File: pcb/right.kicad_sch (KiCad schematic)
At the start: 119 parts, among them J201 OLED 0.96in I2C, Q201 AO3401A, Q202 AO3401A, Q203 AO3400A, SW201 -, SW202 0, SW203 9, SW204 8, SW205 7, SW206 6, SW208 \, SW209 P, SW210 O, SW211 I, SW212 U, SW213 Y, SW214 ', SW215 ;, SW216 L, SW217 K, SW218 J, SW219 H, SW220 Alt, SW221 Shift, SW222 /, SW223 ., SW224 ,, SW225 M, SW226 N, SW227 Ctrl, SW228 ], SW229 [, SW230 Down, SW231 Up, SW232 Fn, SW233 Space, SW234 Enter, SW290 MSK12C02 power, SW291 Reset, U201 nRF52840 Pro Micro

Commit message: feat(layout): refine thumb cluster and OLED placement
Use 1.25u lower thumb keys, keep the upper pair at 1u, move the encoders and OLEDs, and align the board outline with the thumb row. Regenerate the routed PCB, case, plate, print sheets, fabrication files, BOM, and documentation.
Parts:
- SW233, SW234: footprint keygen:SW_MX_HS_CPG151101S11_1.5u -> keygen:SW_MX_HS_CPG151101S11_1.25u
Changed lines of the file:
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@@
     (property "Reference" "SW233" (at 233.68 156.21 0) (effects (font (size 1.27 1.27))))
     (property "Value" "Space" (at 233.68 168.91 0) (effects (font (size 1.27 1.27))))
-    (property "Footprint" "keygen:SW_MX_HS_CPG151101S11_1.5u"
+    (property "Footprint" "keygen:SW_MX_HS_CPG151101S11_1.25u"
       (at 233.68 162.56 0)
       (effects (font (size 1.27 1.27)) (hide yes))
@@
     (property "Reference" "SW234" (at 274.32 156.21 0) (effects (font (size 1.27 1.27))))
     (property "Value" "Enter" (at 274.32 168.91 0) (effects (font (size 1.27 1.27))))
-    (property "Footprint" "keygen:SW_MX_HS_CPG151101S11_1.5u"
+    (property "Footprint" "keygen:SW_MX_HS_CPG151101S11_1.25u"
       (at 274.32 162.56 0)
       (effects (font (size 1.27 1.27)) (hide yes))

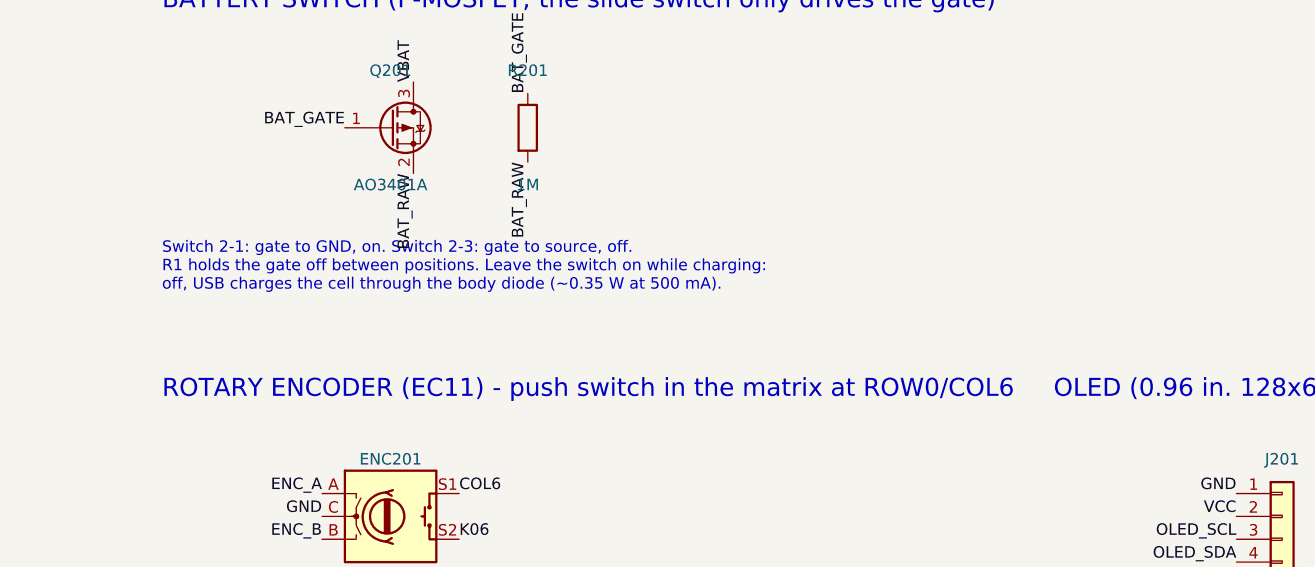
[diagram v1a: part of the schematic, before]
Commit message: chore(hardware): audit power, lighting, and assembly
Verify switch and LED geometry, net connectivity, firmware lighting behavior, and current limits. Record prototype checks and update build guidance and generated assets.
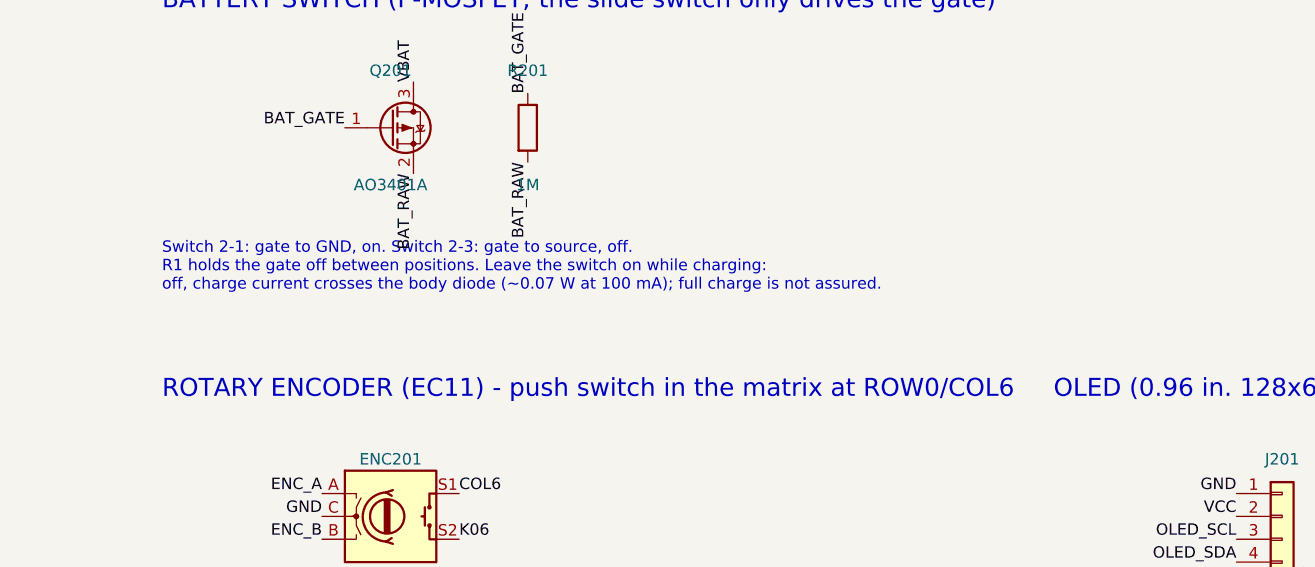
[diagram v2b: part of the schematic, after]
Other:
- note added: "Switch 2-1: gate to GND, on. Switch 2-3: gate to source, off. R1 holds the gate off between positions. Leave the switch on while charging: off, charge current crosses the body diode (~0.07 W at 100 mA); full charge is not assured."
- note removed: "Switch 2-1: gate to GND, on. Switch 2-3: gate to source, off. R1 holds the gate off between positions. Leave the switch on while charging: off, USB charges the cell through the body diode (~0.35 W at 500 mA)."
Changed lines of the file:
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@@
     (effects (font (size 1.27 1.27)) (justify right bottom))
   )
-  (text "Switch 2-1: gate to GND, on. Switch 2-3: gate to source, off.\nR1 holds the gate off between positions. Leave the switch on while charging:\noff, USB charges the cell through the body diode (~0.35 W at 500 mA)."
+  (text "Switch 2-1: gate to GND, on. Switch 2-3: gate to source, off.\nR1 holds the gate off between positions. Leave the switch on while charging:\noff, charge current crosses the body diode (~0.07 W at 100 mA); full charge is not assured."
     (exclude_from_sim no)
     (at 335.28 198.12 0)
